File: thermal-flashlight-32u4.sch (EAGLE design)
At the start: 29 parts, among them IC1 ATMEGA328P, IC2 MCP73831, IC4 MCP1700-33, J1 AYZ0202, Q4 BSS123, U1 MLX90614_, X1 USBSMD

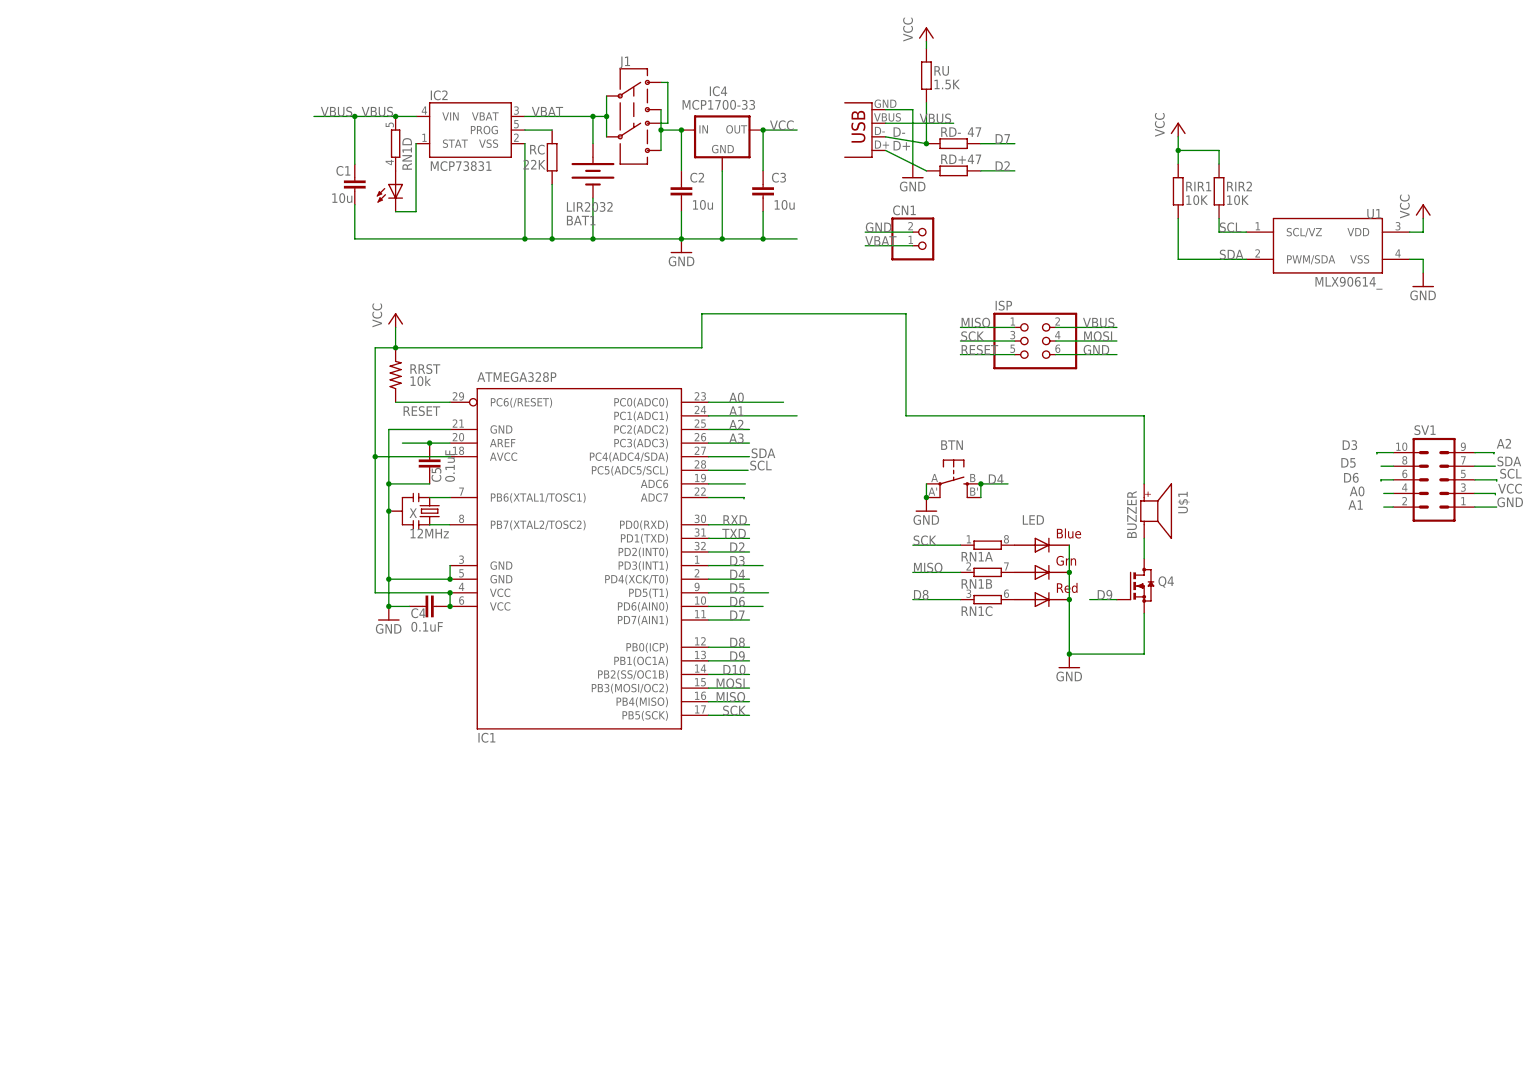
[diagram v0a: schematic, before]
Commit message: added 32u4
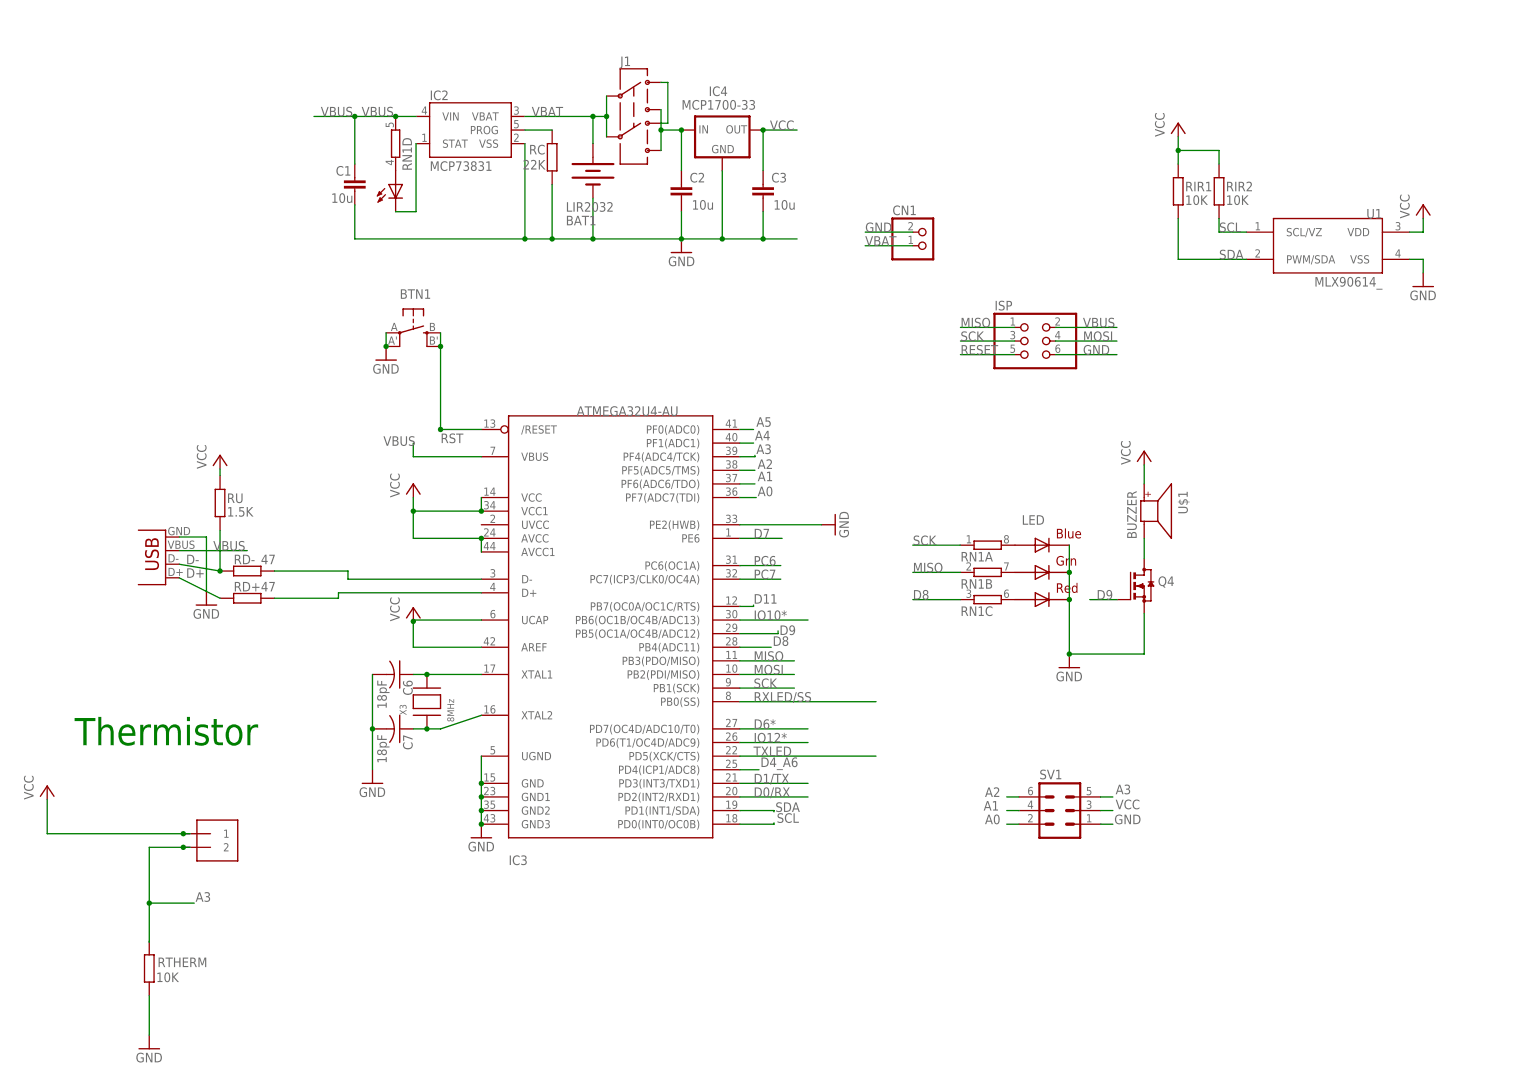
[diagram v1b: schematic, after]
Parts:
- removed BTN: EVQQ2, adafruit:EVQQ2
- removed C4, C5: 0.1uF, rcl:C-EUC0805
- removed IC1: ATMEGA328P, atmel:MEGA8-AI
- removed RRST: 10k, rcl:R-US_R0805
- removed X: 12MHz, SparkFunNew:RESONATORSMD
- added BTN1: EVQQ2, adafruit:EVQQ2
- added C6, C7: 18pF, adafruit:C-USC0805K
- added IC3: ATMEGA32U4-AU, adaprog:ATMEGA32U4-AU
- added J2: 1X2-3.5MM, adafruit:1X2-3.5MM
- added RTHERM: 10K, rcl:R-EU_R0805
- added X3: 8MHz, adaprog:XTALNX5032
- SV1: device con-lstb:MA05-2 -> con-lstb:MA03-2
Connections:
- removed net AREF: C5.2, IC1.AREF
- removed net D10: IC1.PB2(SS/OC1B)
- removed net D2: IC1.PD2(INT0), RD+.2
- removed net D3: IC1.PD3(INT1), SV1.10
- removed net D4: BTN.S, BTN.S1, IC1.PD4(XCK/T0)
- removed net D5: IC1.PD5(T1), SV1.8
- removed net D6: IC1.PD6(AIN0), SV1.6
- removed net N$12: IC1.ADC6
- removed net N$13: IC1.ADC7
- removed net N$2: IC1.PB6(XTAL1/TOSC1), X.1
- removed net N$3: IC1.PB7(XTAL2/TOSC2), X.3
- removed net RXD: IC1.PD0(RXD)
- removed net TXD: IC1.PD1(TXD)
- new net A4: IC3.PF1(ADC1)
- new net A5: IC3.PF0(ADC0)
- new net D0/RX: IC3.PD2(INT2/RXD1)
- new net D1/TX: IC3.PD3(INT3/TXD1)
- new net D11: IC3.PB7(OC0A/OC1C/RTS)
- new net D4_A6: IC3.PD4(ICP1/ADC8)
- new net D6*: IC3.PD7(OC4D/ADC10/T0)
- new net IO10*: IC3.PB6(OC1B/OC4B/ADC13)
- new net IO12*: IC3.PD6(T1/OC4D/ADC9)
- new net N$11: IC3.D+, RD+.2
- new net N$15: C7.1, IC3.XTAL2, X3.P$1
- new net N$16: C6.1, IC3.XTAL1, X3.P$2
- new net N$18: IC3.D-, RD-.2
- new net PC6: IC3.PC6(OC1A)
- new net PC7: IC3.PC7(ICP3/CLK0/OC4A)
- new net RST: BTN1.S, BTN1.S1, IC3./RESET
- new net RXLED/SS: IC3.PB0(SS)
- new net TXLED: IC3.PD5(XCK/CTS)
- net A0: now also IC3.PF7(ADC7(TDI), SV1.2; no longer IC1.PC0(ADC0), SV1.4
- net A1: now also IC3.PF6(ADC6/TDO), SV1.4; no longer IC1.PC1(ADC1), SV1.2
- net A2: now also IC3.PF5(ADC5/TMS), SV1.6; no longer IC1.PC2(ADC2), SV1.9
- net A3: now also IC3.PF4(ADC4/TCK), J2.2, RTHERM.2, SV1.5; no longer IC1.PC3(ADC3)
- net D7: now also IC3.PE6; no longer IC1.PD7(AIN1), RD-.2
- net D8: now also IC3.PB4(ADC11); no longer IC1.PB0(ICP)
- net D9: now also IC3.PB5(OC1A/OC4B/ADC12); no longer IC1.PB1(OC1A)
- net GND: now also BTN1.P, BTN1.P1, C6.2, C7.2, IC3.GND, IC3.GND1, IC3.GND2, IC3.GND3, IC3.PE2(HWB), IC3.UGND, RTHERM.1; no longer BTN.P, BTN.P1, C4.1, C5.1, IC1.GND, IC1.GND@1, IC1.GND@2, X.2
- net MISO: now also IC3.PB3(PDO/MISO); no longer IC1.PB4(MISO)
- net MOSI: now also IC3.PB2(PDI/MISO); no longer IC1.PB3(MOSI/OC2)
- net RESET: no longer IC1.PC6(/RESET), RRST.1
- net SCK: now also IC3.PB1(SCK); no longer IC1.PB5(SCK)
- net SCL: now also IC3.PD0(INT0/OC0B); no longer IC1.PC5(ADC5/SCL), SV1.5
- net SDA: now also IC3.PD1(INT1/SDA); no longer IC1.PC4(ADC4/SDA), SV1.7
- net VBUS: now also IC3.VBUS
- net VCC: now also IC3.AREF, IC3.AVCC, IC3.AVCC1, IC3.UCAP, IC3.VCC, IC3.VCC1, J2.1; no longer C4.2, IC1.AVCC, IC1.VCC@1, IC1.VCC@2, RRST.2
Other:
- note added: "Thermistor"
- moved on the sheet: RD+, RD-, RU

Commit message: update
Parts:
- renumbered BTN1 to BTN
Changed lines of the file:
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@@
 <part name="GND15" library="supply1" deviceset="GND" device=""/>
 <part name="GND16" library="supply1" deviceset="GND" device=""/>
-<part name="BTN1" library="adafruit" deviceset="EVQQ2" device="" value=""/>
+<part name="BTN" library="adafruit" deviceset="EVQQ2" device="" value=""/>
 <part name="P+6" library="supply1" deviceset="VCC" device=""/>
 <part name="P+8" library="supply1" deviceset="VCC" device=""/>
@@
 <sheet>
 <plain>
-<text x="-21.844" y="3.302" size="5.08" layer="91" rot="R180">Thermistor</text>
+<text x="-30.226" y="-8.89" size="2.1844" layer="91" rot="R180">Thermistor</text>
 </plain>
 <instances>
@@
 <instance part="GND15" gate="1" x="85.852" y="39.37" rot="MR270"/>
 <instance part="GND16" gate="1" x="2.032" y="70.104"/>
-<instance part="BTN1" gate="G$1" x="7.112" y="75.184" rot="R270"/>
+<instance part="BTN" gate="G$1" x="7.112" y="75.184" rot="R270"/>
 <instance part="P+6" gate="VCC" x="7.112" y="46.99"/>
 <instance part="P+8" gate="VCC" x="7.112" y="23.876"/>
@@
 <junction x="2.032" y="72.644"/>
 <pinref part="GND16" gate="1" pin="GND"/>
-<pinref part="BTN1" gate="G$1" pin="P1"/>
-<pinref part="BTN1" gate="G$1" pin="P"/>
+<pinref part="BTN" gate="G$1" pin="P1"/>
+<pinref part="BTN" gate="G$1" pin="P"/>
 </segment>
 <segment>
@@
 <wire x1="12.192" y1="57.15" x2="12.192" y2="72.644" width="0.1524" layer="91"/>
 <junction x="12.192" y="57.15"/>
-<pinref part="BTN1" gate="G$1" pin="S"/>
-<pinref part="BTN1" gate="G$1" pin="S1"/>
+<pinref part="BTN" gate="G$1" pin="S"/>
+<pinref part="BTN" gate="G$1" pin="S1"/>
 <wire x1="12.192" y1="75.184" x2="12.192" y2="72.644" width="0.1524" layer="91"/>
 <junction x="12.192" y="72.644"/>

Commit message: update
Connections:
- net A3: no longer J2.2, RTHERM.2
- net A4: now also J2.2, RTHERM.2
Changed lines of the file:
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@@
 <part name="GND1" library="SparkFun" deviceset="GND" device=""/>
 <part name="RTHERM" library="rcl" deviceset="R-EU_" device="R0805" value="10K"/>
-<part name="P+5" library="supply1" deviceset="VCC" device=""/>
 <part name="GND9" library="supply1" deviceset="GND" device=""/>
 <part name="GND10" library="supply1" deviceset="GND" device=""/>
@@
 <part name="P+1" library="supply1" deviceset="VCC" device=""/>
 <part name="SV1" library="con-lstb" deviceset="MA03-2" device=""/>
+<part name="P+7" library="supply1" deviceset="VCC" device=""/>
 </parts>
 <sheets>
@@
 <attribute name="VALUE" x="158.75" y="99.06" size="1.778" layer="96"/>
 </instance>
-<instance part="J2" gate="G$1" x="-30.734" y="-20.828"/>
+<instance part="J2" gate="G$1" x="-30.988" y="-20.828"/>
 <instance part="GND1" gate="1" x="-42.164" y="-58.42"/>
 <instance part="RTHERM" gate="G$1" x="-42.164" y="-43.434" smashed="yes" rot="R90">
@@
 <attribute name="VALUE" x="-40.894" y="-45.974" size="1.778" layer="96"/>
 </instance>
-<instance part="P+5" gate="VCC" x="-61.214" y="-9.398"/>
 <instance part="GND9" gate="1" x="19.812" y="-19.05"/>
 <instance part="GND10" gate="1" x="-0.508" y="-8.89"/>
@@
 <instance part="P+1" gate="VCC" x="143.51" y="53.086"/>
 <instance part="SV1" gate="1" x="127.762" y="-13.97"/>
+<instance part="P+7" gate="VCC" x="-47.752" y="-18.288" rot="R90"/>
 </instances>
 <busses>
@@
 </segment>
 <segment>
-<wire x1="-34.544" y1="-18.288" x2="-35.814" y2="-18.288" width="0.1524" layer="91"/>
-<pinref part="J2" gate="G$1" pin="1"/>
-<wire x1="-35.814" y1="-18.288" x2="-61.214" y2="-18.288" width="0.1524" layer="91"/>
-<junction x="-35.814" y="-18.288"/>
-<wire x1="-61.214" y1="-18.288" x2="-61.214" y2="-11.938" width="0.1524" layer="91"/>
-<pinref part="P+5" gate="VCC" pin="VCC"/>
-</segment>
-<segment>
 <wire x1="19.812" y1="41.91" x2="19.812" y2="44.45" width="0.1524" layer="91"/>
 <wire x1="7.112" y1="41.91" x2="19.812" y2="41.91" width="0.1524" layer="91"/>
@@
 <label x="138.176" y="-13.716" size="1.778" layer="95"/>
 </segment>
+<segment>
+<pinref part="J2" gate="G$1" pin="1"/>
+<pinref part="P+7" gate="VCC" pin="VCC"/>
+<wire x1="-45.212" y1="-18.288" x2="-36.068" y2="-18.288" width="0.1524" layer="91"/>
+</segment>
 </net>
 <net name="SCK" class="0">
@@
 </net>
 <net name="A3" class="0">
-<segment>
-<wire x1="-34.544" y1="-20.828" x2="-35.814" y2="-20.828" width="0.1524" layer="91"/>
-<wire x1="-35.814" y1="-20.828" x2="-42.164" y2="-20.828" width="0.1524" layer="91"/>
-<wire x1="-42.164" y1="-20.828" x2="-42.164" y2="-31.242" width="0.1524" layer="91"/>
-<pinref part="J2" gate="G$1" pin="2"/>
-<junction x="-35.814" y="-20.828"/>
-<pinref part="RTHERM" gate="G$1" pin="2"/>
-<wire x1="-42.164" y1="-31.242" x2="-42.164" y2="-38.354" width="0.1524" layer="91"/>
-<wire x1="-42.164" y1="-38.354" x2="-42.164" y2="-38.608" width="0.1524" layer="91"/>
-<wire x1="-42.164" y1="-31.242" x2="-33.782" y2="-31.242" width="0.1524" layer="91"/>
-<junction x="-42.164" y="-31.242"/>
-<label x="-33.528" y="-30.988" size="1.778" layer="95"/>
-</segment>
 <segment>
 <pinref part="IC3" gate="G$1" pin="PF4(ADC4/TCK)"/>
@@
 <label x="70.866" y="55.118" size="1.778" layer="95"/>
 </segment>
-</net>
+<segment>
+<pinref part="RTHERM" gate="G$1" pin="2"/>
+<wire x1="-42.164" y1="-38.354" x2="-42.164" y2="-32.766" width="0.1524" layer="91"/>
+<wire x1="-42.164" y1="-32.766" x2="-42.164" y2="-20.828" width="0.1524" layer="91"/>
+<wire x1="-42.164" y1="-20.828" x2="-36.068" y2="-20.828" width="0.1524" layer="91"/>
+<pinref part="J2" gate="G$1" pin="2"/>
+<wire x1="-42.164" y1="-32.766" x2="-37.846" y2="-32.766" width="0.1524" layer="91"/>
+<junction x="-42.164" y="-32.766"/>
+<label x="-36.068" y="-32.766" size="1.778" layer="95"/>
+</segment>
+</net>

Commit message: update
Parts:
- added LED1: RGBLED5050, adafruit:RGBLED5050
- added RN2: (no value), resistor-dil:4R-NEXB38V
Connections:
- new net N$12: LED1.RED_A, RN2C.2
- new net N$2: LED1.BLUE_A, RN2A.2
- new net N$3: LED1.GREEN_A, RN2B.2
- net D8: now also RN2C.1
- net GND: now also LED1.BLUE_C, LED1.GREEN_C, LED1.RED_C
- net MISO: now also RN2B.1
- net SCK: now also RN2A.1
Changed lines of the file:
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@@
 <setting verticaltext="up"/>
 </settings>
-<grid distance="0.01" unitdist="inch" unit="inch" style="lines" multiple="1" display="no" altdistance="0.01" altunitdist="inch" altunit="inch"/>
+<grid distance="0.1" unitdist="inch" unit="inch" style="lines" multiple="1" display="no" altdistance="0.01" altunitdist="inch" altunit="inch"/>
 <layers>
 <layer number="1" name="Top" color="4" fill="1" visible="no" active="no"/>
@@
 <part name="SV1" library="con-lstb" deviceset="MA03-2" device=""/>
 <part name="P+7" library="supply1" deviceset="VCC" device=""/>
+<part name="LED1" library="adafruit" deviceset="RGBLED" device="5050"/>
+<part name="RN2" library="resistor-dil" deviceset="4R-N" device="EXB38V"/>
+<part name="GND3" library="supply1" deviceset="GND" device=""/>
 </parts>
 <sheets>
@@
 <instance part="SV1" gate="1" x="127.762" y="-13.97"/>
 <instance part="P+7" gate="VCC" x="-47.752" y="-18.288" rot="R90"/>
+<instance part="LED1" gate="G$1" x="185.42" y="30.48"/>
+<instance part="RN2" gate="A" x="175.26" y="35.56"/>
+<instance part="RN2" gate="B" x="175.26" y="30.48"/>
+<instance part="RN2" gate="C" x="175.26" y="25.4"/>
+<instance part="GND3" gate="1" x="190.5" y="15.24"/>
 </instances>
 <busses>
@@
 <label x="137.922" y="-16.51" size="1.778" layer="95"/>
 </segment>
+<segment>
+<pinref part="LED1" gate="G$1" pin="BLUE_C"/>
+<pinref part="LED1" gate="G$1" pin="GREEN_C"/>
+<wire x1="190.5" y1="35.56" x2="190.5" y2="30.48" width="0.1524" layer="91"/>
+<pinref part="LED1" gate="G$1" pin="RED_C"/>
+<wire x1="190.5" y1="30.48" x2="190.5" y2="25.4" width="0.1524" layer="91"/>
+<junction x="190.5" y="30.48"/>
+<wire x1="190.5" y1="25.4" x2="190.5" y2="17.78" width="0.1524" layer="91"/>
+<junction x="190.5" y="25.4"/>
+<pinref part="GND3" gate="1" pin="GND"/>
+</segment>
 </net>
 <net name="VBUS" class="0">
@@
 <pinref part="IC3" gate="G$1" pin="PB1(SCK)"/>
 </segment>
+<segment>
+<wire x1="170.18" y1="35.56" x2="161.29" y2="35.56" width="0.1524" layer="91"/>
+<label x="161.29" y="35.56" size="1.778" layer="95"/>
+<pinref part="RN2" gate="A" pin="1"/>
+</segment>
 </net>
 <net name="MISO" class="0">
@@
 <label x="70.612" y="13.97" size="1.778" layer="95"/>
 <pinref part="IC3" gate="G$1" pin="PB3(PDO/MISO)"/>
+</segment>
+<segment>
+<wire x1="170.18" y1="30.48" x2="161.29" y2="30.48" width="0.1524" layer="91"/>
+<label x="161.29" y="30.48" size="1.778" layer="95"/>
+<pinref part="RN2" gate="B" pin="1"/>
 </segment>
 </net>
@@
 <wire x1="68.072" y1="16.51" x2="73.914" y2="16.51" width="0.1524" layer="91"/>
 <label x="74.168" y="16.764" size="1.778" layer="95"/>
+</segment>
+<segment>
+<wire x1="170.18" y1="25.4" x2="161.29" y2="25.4" width="0.1524" layer="91"/>
+<label x="161.29" y="25.4" size="1.778" layer="95"/>
+<pinref part="RN2" gate="C" pin="1"/>
 </segment>
 </net>
@@
 </segment>
 </net>
+<net name="N$2" class="0">
+<segment>
+<pinref part="LED1" gate="G$1" pin="BLUE_A"/>
+<pinref part="RN2" gate="A" pin="2"/>
+</segment>
+</net>
+<net name="N$3" class="0">
+<segment>
+<pinref part="LED1" gate="G$1" pin="GREEN_A"/>
+<pinref part="RN2" gate="B" pin="2"/>
+</segment>
+</net>
+<net name="N$12" class="0">
+<segment>
+<pinref part="LED1" gate="G$1" pin="RED_A"/>
+<pinref part="RN2" gate="C" pin="2"/>
+</segment>
+</net>
